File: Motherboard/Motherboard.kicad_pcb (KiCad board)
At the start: 2 copper layers, 75 x 75 mm, 43 parts, among them J1 AUX Analog A, J10 Moisture 4, J11 Moisture 5, J12 Power In, J2 AUX Analog B, J3 RPi 3B+, J4 AUX Digital A, J5 AUX Digital B, J6 Moisture 0, J7 Moisture 1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

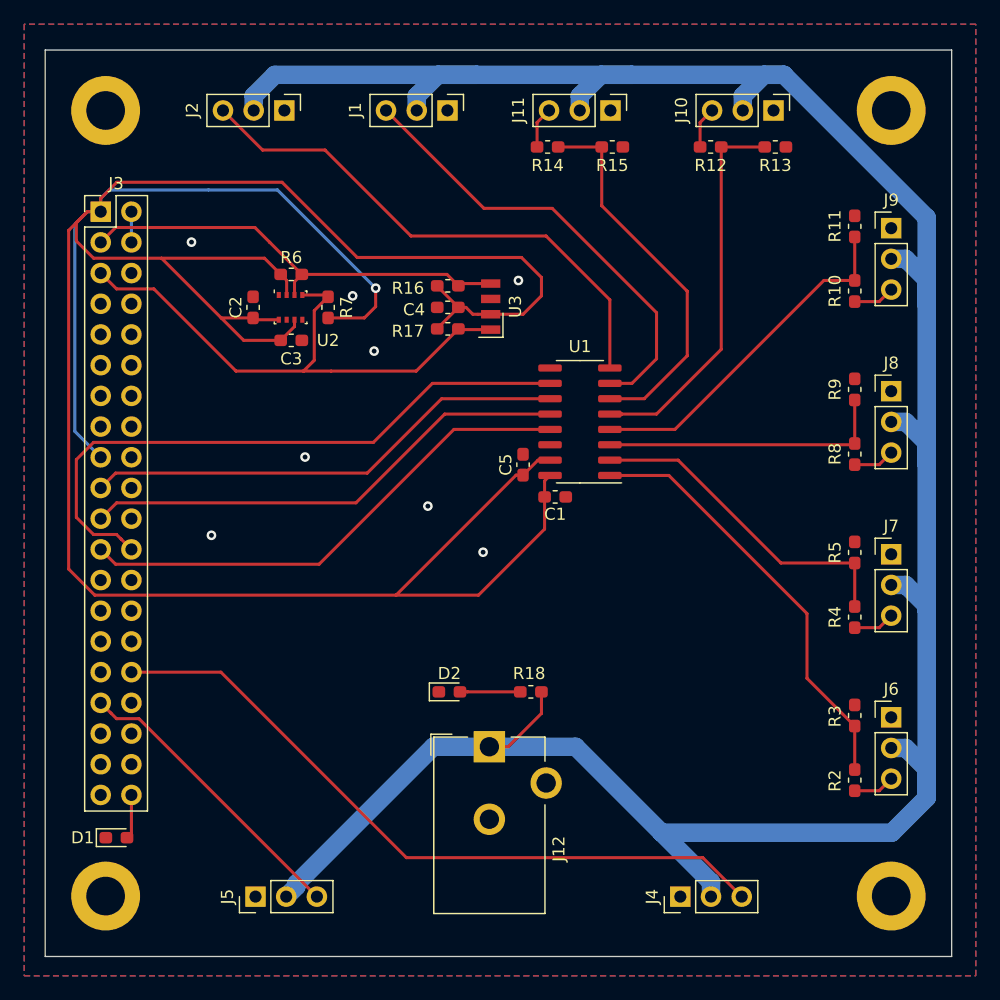
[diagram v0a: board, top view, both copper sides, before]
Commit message: add silk screen
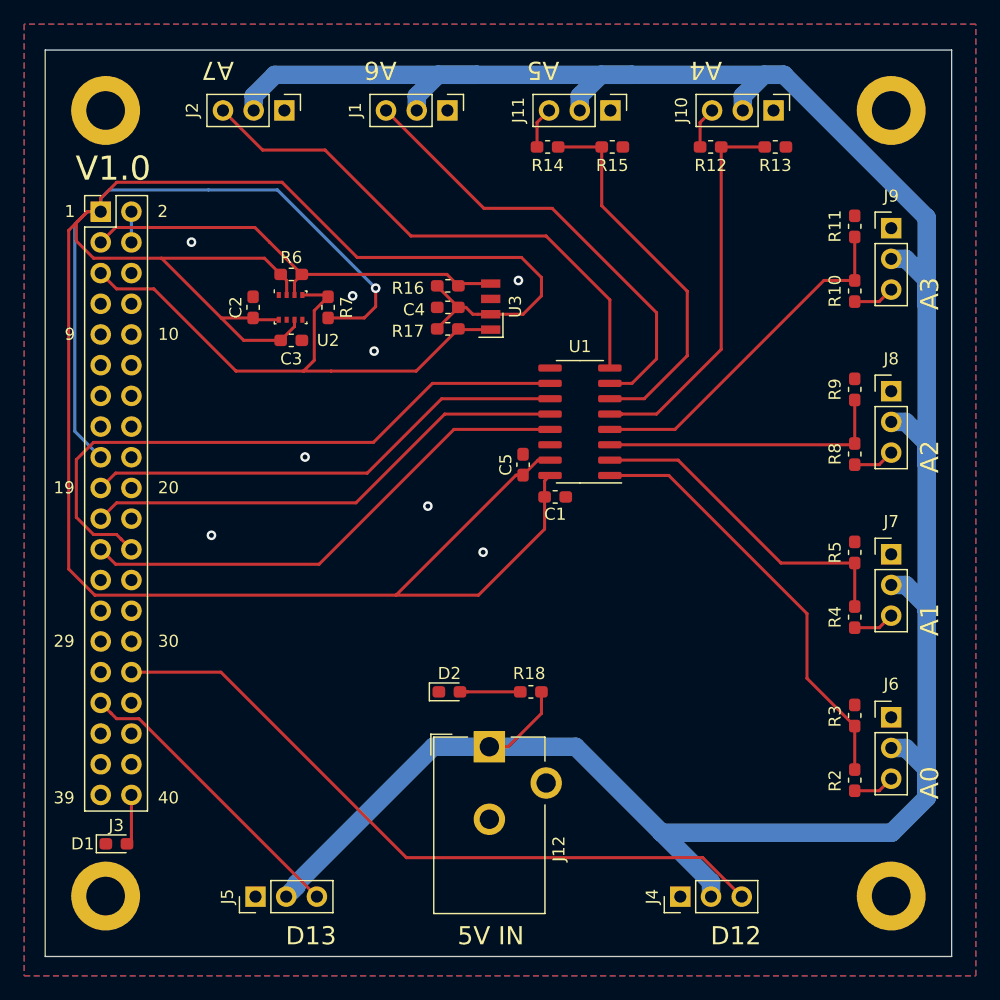
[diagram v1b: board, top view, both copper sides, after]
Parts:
- moved D1 0.51 mm to (55.9, 90.7)
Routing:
- net GPIO_21: track 3.69 -> 4.20 mm
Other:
- board text added: "1"
- board text added: "10"
- board text added: "19"
- board text added: "2"
- board text added: "20"
- board text added: "29"
- board text added: "30"
- board text added: "39"
- board text added: "40"
- board text added: "5V IN"
- board text added: "9"
- board text added: "A0"
- board text added: "A1"
- board text added: "A2"
- board text added: "A3"
- board text added: "A4"
- board text added: "A5"
- board text added: "A6"
- board text added: "A7"
- board text added: "D12"
- board text added: "D13"
- board text added: "V1.0"
